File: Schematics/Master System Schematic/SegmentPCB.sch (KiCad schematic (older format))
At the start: 28 parts, among them K13 Voltage Tap Relay, K14 Voltage Tap Relay, K15 Voltage Tap Relay, K16 Voltage Tap Relay, K17 Voltage Tap Relay, K18 Voltage Tap Relay, K19 Voltage Tap Relay, K20 Voltage Tap Relay, K21 Voltage Tap Relay, K22 Voltage Tap Relay

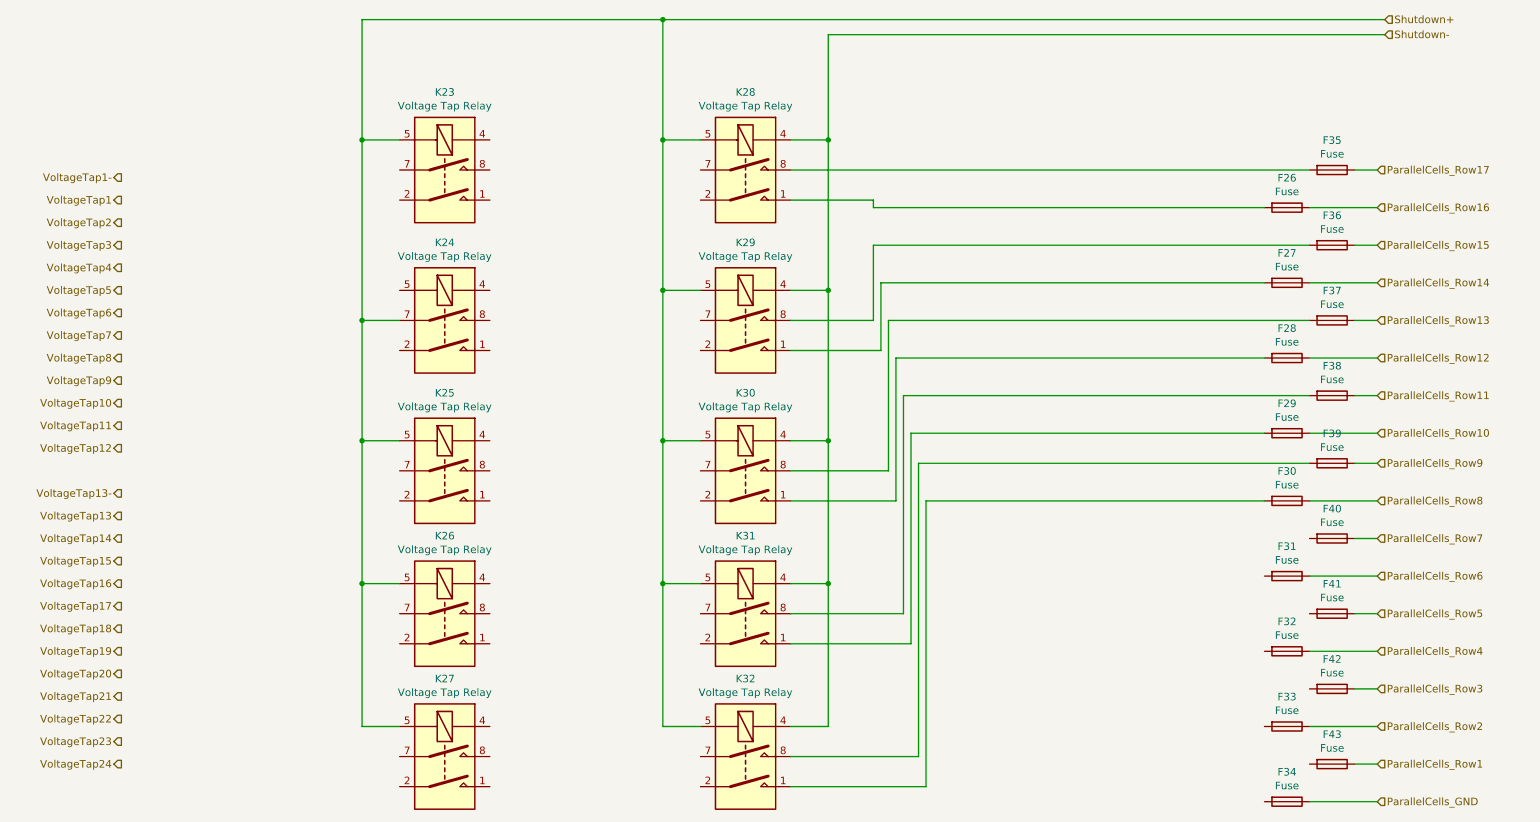
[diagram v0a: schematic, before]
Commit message: Clean up for merge
>cleaned wire runs on top sheet
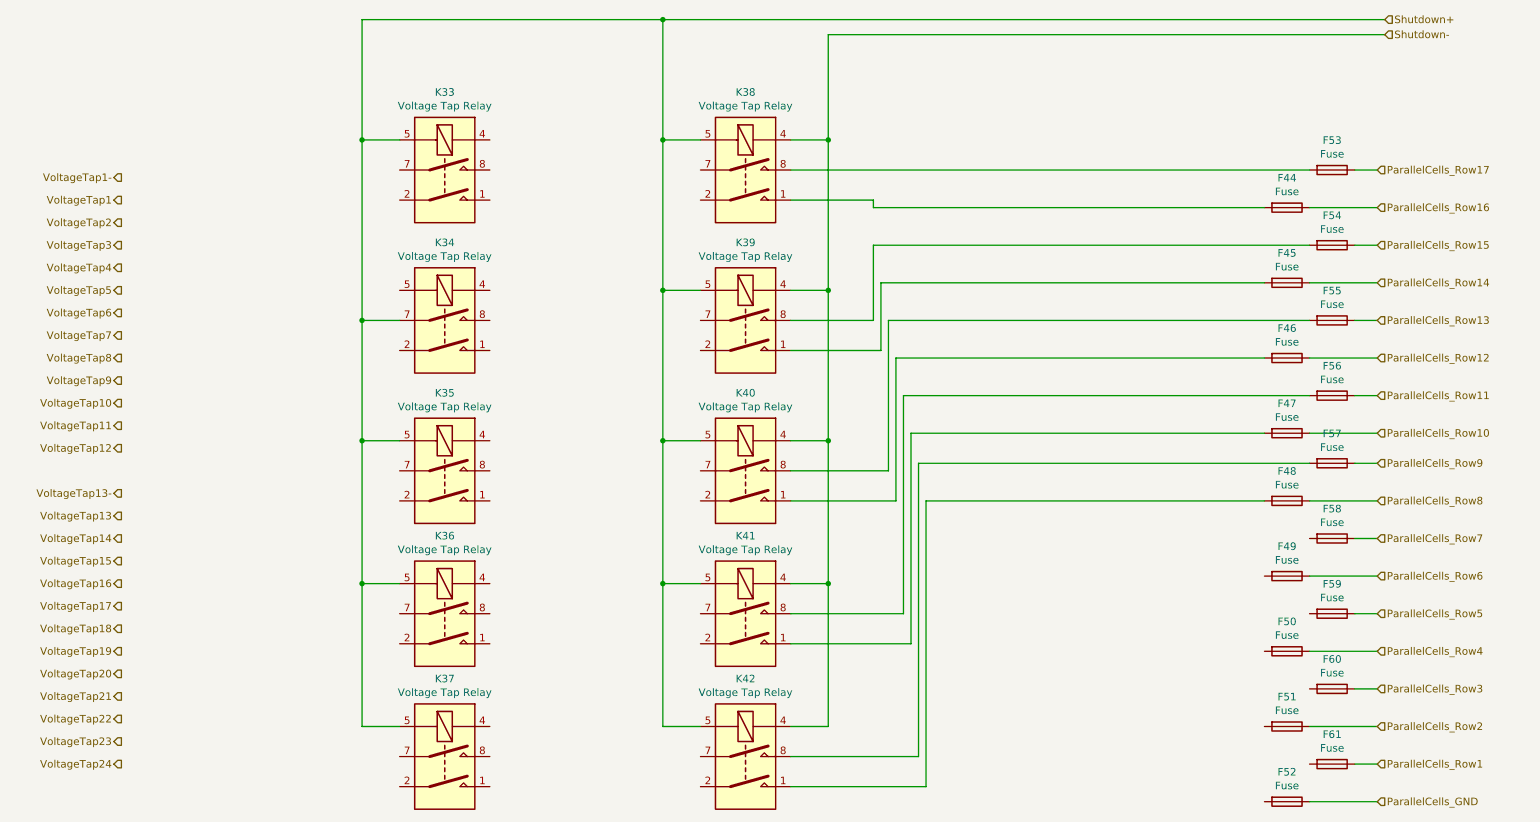
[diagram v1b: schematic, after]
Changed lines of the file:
@@
 EESchema Schematic File Version 4
-LIBS:Master System Schematic-cache
 EELAYER 30 0
 EELAYER END
@@
 AR Path="/5F45B05E/604E5331/6054192C" Ref="K33"  Part="1"
 AR Path="/5F45B05E/604E5333/6054192C" Ref="K43"  Part="1"
-F 0 "K23" H 3650 2367 50  0000 C CNN
+F 0 "K33" H 3650 2367 50  0000 C CNN
 F 1 "Voltage Tap Relay" H 3650 2276 50  0000 C CNN
 F 2 "Relay_THT:Relay_DPST_Fujitsu_FTR-F1A" H 3650 1450 50  0001 C CNN
@@
 AR Path="/5F45B05E/604E5331/60548E5D" Ref="K38"  Part="1"
 AR Path="/5F45B05E/604E5333/60548E5D" Ref="K48"  Part="1"
-F 0 "K28" H 5650 2367 50  0000 C CNN
+F 0 "K38" H 5650 2367 50  0000 C CNN
 F 1 "Voltage Tap Relay" H 5650 2276 50  0000 C CNN
 F 2 "Relay_THT:Relay_DPST_Fujitsu_FTR-F1A" H 5650 1450 50  0001 C CNN
@@
 AR Path="/5F45B05E/604E5331/6054A887" Ref="K39"  Part="1"
 AR Path="/5F45B05E/604E5333/6054A887" Ref="K49"  Part="1"
-F 0 "K29" H 5650 3367 50  0000 C CNN
+F 0 "K39" H 5650 3367 50  0000 C CNN
 F 1 "Voltage Tap Relay" H 5650 3276 50  0000 C CNN
 F 2 "Relay_THT:Relay_DPST_Fujitsu_FTR-F1A" H 5650 2450 50  0001 C CNN
@@
 AR Path="/5F45B05E/604E5331/6054A88D" Ref="K40"  Part="1"
 AR Path="/5F45B05E/604E5333/6054A88D" Ref="K50"  Part="1"
-F 0 "K30" H 5650 4367 50  0000 C CNN
+F 0 "K40" H 5650 4367 50  0000 C CNN
 F 1 "Voltage Tap Relay" H 5650 4276 50  0000 C CNN
 F 2 "Relay_THT:Relay_DPST_Fujitsu_FTR-F1A" H 5650 3450 50  0001 C CNN
@@
 AR Path="/5F45B05E/604E5331/6054A893" Ref="K41"  Part="1"
 AR Path="/5F45B05E/604E5333/6054A893" Ref="K51"  Part="1"
-F 0 "K31" H 5650 5317 50  0000 C CNN
+F 0 "K41" H 5650 5317 50  0000 C CNN
 F 1 "Voltage Tap Relay" H 5650 5226 50  0000 C CNN
 F 2 "Relay_THT:Relay_DPST_Fujitsu_FTR-F1A" H 5650 4400 50  0001 C CNN
@@
 AR Path="/5F45B05E/604E5331/6054A899" Ref="K42"  Part="1"
 AR Path="/5F45B05E/604E5333/6054A899" Ref="K52"  Part="1"
-F 0 "K32" H 5650 6267 50  0000 C CNN
+F 0 "K42" H 5650 6267 50  0000 C CNN
 F 1 "Voltage Tap Relay" H 5650 6176 50  0000 C CNN
 F 2 "Relay_THT:Relay_DPST_Fujitsu_FTR-F1A" H 5650 5350 50  0001 C CNN
@@
 AR Path="/5F45B05E/604E5331/6057568E" Ref="F53"  Part="1"
 AR Path="/5F45B05E/604E5333/6057568E" Ref="F71"  Part="1"
-F 0 "F35" V 9353 1850 50  0000 C CNN
+F 0 "F53" V 9353 1850 50  0000 C CNN
 F 1 "Fuse" V 9444 1850 50  0000 C CNN
 F 2 "" V 9480 1850 50  0001 C CNN
@@
 AR Path="/5F45B05E/604E5331/6057794E" Ref="F54"  Part="1"
 AR Path="/5F45B05E/604E5333/6057794E" Ref="F72"  Part="1"
-F 0 "F36" V 9353 2350 50  0000 C CNN
+F 0 "F54" V 9353 2350 50  0000 C CNN
 F 1 "Fuse" V 9444 2350 50  0000 C CNN
 F 2 "" V 9480 2350 50  0001 C CNN
@@
 AR Path="/5F45B05E/604E5331/60577954" Ref="F45"  Part="1"
 AR Path="/5F45B05E/604E5333/60577954" Ref="F63"  Part="1"
-F 0 "F27" V 9053 2600 50  0000 C CNN
+F 0 "F45" V 9053 2600 50  0000 C CNN
 F 1 "Fuse" V 9144 2600 50  0000 C CNN
 F 2 "" V 9180 2600 50  0001 C CNN
@@
 AR Path="/5F45B05E/604E5331/60579EA8" Ref="F55"  Part="1"
 AR Path="/5F45B05E/604E5333/60579EA8" Ref="F73"  Part="1"
-F 0 "F37" V 9353 2850 50  0000 C CNN
+F 0 "F55" V 9353 2850 50  0000 C CNN
 F 1 "Fuse" V 9444 2850 50  0000 C CNN
 F 2 "" V 9480 2850 50  0001 C CNN
@@
 AR Path="/5F45B05E/604E5331/60579EAE" Ref="F46"  Part="1"
 AR Path="/5F45B05E/604E5333/60579EAE" Ref="F64"  Part="1"
-F 0 "F28" V 9053 3100 50  0000 C CNN
+F 0 "F46" V 9053 3100 50  0000 C CNN
 F 1 "Fuse" V 9144 3100 50  0000 C CNN
 F 2 "" V 9180 3100 50  0001 C CNN
@@
 AR Path="/5F45B05E/604E5331/60579EB6" Ref="F56"  Part="1"
 AR Path="/5F45B05E/604E5333/60579EB6" Ref="F74"  Part="1"
-F 0 "F38" V 9353 3350 50  0000 C CNN
+F 0 "F56" V 9353 3350 50  0000 C CNN
 F 1 "Fuse" V 9444 3350 50  0000 C CNN
 F 2 "" V 9480 3350 50  0001 C CNN
@@
 AR Path="/5F45B05E/604E5331/60579EBC" Ref="F47"  Part="1"
 AR Path="/5F45B05E/604E5333/60579EBC" Ref="F65"  Part="1"
-F 0 "F29" V 9053 3600 50  0000 C CNN
+F 0 "F47" V 9053 3600 50  0000 C CNN
 F 1 "Fuse" V 9144 3600 50  0000 C CNN
 F 2 "" V 9180 3600 50  0001 C CNN
@@
 AR Path="/5F45B05E/604E5331/6057BB2B" Ref="F57"  Part="1"
 AR Path="/5F45B05E/604E5333/6057BB2B" Ref="F75"  Part="1"
-F 0 "F39" V 9353 3800 50  0000 C CNN
+F 0 "F57" V 9353 3800 50  0000 C CNN
 F 1 "Fuse" V 9444 3800 50  0000 C CNN
 F 2 "" V 9480 3800 50  0001 C CNN
@@
 AR Path="/5F45B05E/604E5331/6057BB31" Ref="F48"  Part="1"
 AR Path="/5F45B05E/604E5333/6057BB31" Ref="F66"  Part="1"
-F 0 "F30" V 9053 4050 50  0000 C CNN
+F 0 "F48" V 9053 4050 50  0000 C CNN
 F 1 "Fuse" V 9144 4050 50  0000 C CNN
 F 2 "" V 9180 4050 50  0001 C CNN
@@
 AR Path="/5F45B05E/604E5331/6057BB39" Ref="F58"  Part="1"
 AR Path="/5F45B05E/604E5333/6057BB39" Ref="F76"  Part="1"
-F 0 "F40" V 9353 4300 50  0000 C CNN
+F 0 "F58" V 9353 4300 50  0000 C CNN
 F 1 "Fuse" V 9444 4300 50  0000 C CNN
 F 2 "" V 9480 4300 50  0001 C CNN
@@
 AR Path="/5F45B05E/604E5331/6057BB3F" Ref="F49"  Part="1"
 AR Path="/5F45B05E/604E5333/6057BB3F" Ref="F67"  Part="1"
-F 0 "F31" V 9053 4550 50  0000 C CNN
+F 0 "F49" V 9053 4550 50  0000 C CNN
 F 1 "Fuse" V 9144 4550 50  0000 C CNN
 F 2 "" V 9180 4550 50  0001 C CNN
@@
 AR Path="/5F45B05E/604E5331/6057BB47" Ref="F59"  Part="1"
 AR Path="/5F45B05E/604E5333/6057BB47" Ref="F77"  Part="1"
-F 0 "F41" V 9353 4800 50  0000 C CNN
+F 0 "F59" V 9353 4800 50  0000 C CNN
 F 1 "Fuse" V 9444 4800 50  0000 C CNN
 F 2 "" V 9480 4800 50  0001 C CNN
@@
 AR Path="/5F45B05E/604E5331/6057BB4D" Ref="F50"  Part="1"
 AR Path="/5F45B05E/604E5333/6057BB4D" Ref="F68"  Part="1"
-F 0 "F32" V 9053 5050 50  0000 C CNN
+F 0 "F50" V 9053 5050 50  0000 C CNN
 F 1 "Fuse" V 9144 5050 50  0000 C CNN
 F 2 "" V 9180 5050 50  0001 C CNN
@@
 AR Path="/5F45B05E/604E5331/6057BB55" Ref="F60"  Part="1"
 AR Path="/5F45B05E/604E5333/6057BB55" Ref="F78"  Part="1"
-F 0 "F42" V 9353 5300 50  0000 C CNN
+F 0 "F60" V 9353 5300 50  0000 C CNN
 F 1 "Fuse" V 9444 5300 50  0000 C CNN
 F 2 "" V 9480 5300 50  0001 C CNN
@@
 AR Path="/5F45B05E/604E5331/6057BB5B" Ref="F51"  Part="1"
 AR Path="/5F45B05E/604E5333/6057BB5B" Ref="F69"  Part="1"
-F 0 "F33" V 9053 5550 50  0000 C CNN
+F 0 "F51" V 9053 5550 50  0000 C CNN
 F 1 "Fuse" V 9144 5550 50  0000 C CNN
 F 2 "" V 9180 5550 50  0001 C CNN
@@
 AR Path="/5F45B05E/604E5331/6057D363" Ref="F61"  Part="1"
 AR Path="/5F45B05E/604E5333/6057D363" Ref="F79"  Part="1"
-F 0 "F43" V 9353 5800 50  0000 C CNN
+F 0 "F61" V 9353 5800 50  0000 C CNN
 F 1 "Fuse" V 9444 5800 50  0000 C CNN
 F 2 "" V 9480 5800 50  0001 C CNN
@@
 AR Path="/5F45B05E/604E5331/6057D369" Ref="F52"  Part="1"
 AR Path="/5F45B05E/604E5333/6057D369" Ref="F70"  Part="1"
-F 0 "F34" V 9053 6050 50  0000 C CNN
+F 0 "F52" V 9053 6050 50  0000 C CNN
 F 1 "Fuse" V 9144 6050 50  0000 C CNN
 F 2 "" V 9180 6050 50  0001 C CNN
@@
 AR Path="/5F45B05E/604E5331/60575FDA" Ref="F44"  Part="1"
 AR Path="/5F45B05E/604E5333/60575FDA" Ref="F62"  Part="1"
-F 0 "F26" V 9053 2100 50  0000 C CNN
+F 0 "F44" V 9053 2100 50  0000 C CNN
 F 1 "Fuse" V 9144 2100 50  0000 C CNN
 F 2 "" V 9180 2100 50  0001 C CNN
@@
 AR Path="/5F45B05E/604E5331/605448E5" Ref="K37"  Part="1"
 AR Path="/5F45B05E/604E5333/605448E5" Ref="K47"  Part="1"
-F 0 "K27" H 3650 6267 50  0000 C CNN
+F 0 "K37" H 3650 6267 50  0000 C CNN
 F 1 "Voltage Tap Relay" H 3650 6176 50  0000 C CNN
 F 2 "Relay_THT:Relay_DPST_Fujitsu_FTR-F1A" H 3650 5350 50  0001 C CNN
@@
 AR Path="/5F45B05E/604E5331/6054435E" Ref="K36"  Part="1"
 AR Path="/5F45B05E/604E5333/6054435E" Ref="K46"  Part="1"
-F 0 "K26" H 3650 5317 50  0000 C CNN
+F 0 "K36" H 3650 5317 50  0000 C CNN
 F 1 "Voltage Tap Relay" H 3650 5226 50  0000 C CNN
 F 2 "Relay_THT:Relay_DPST_Fujitsu_FTR-F1A" H 3650 4400 50  0001 C CNN
@@
 AR Path="/5F45B05E/604E5331/60543EA1" Ref="K35"  Part="1"
 AR Path="/5F45B05E/604E5333/60543EA1" Ref="K45"  Part="1"
-F 0 "K25" H 3650 4367 50  0000 C CNN
+F 0 "K35" H 3650 4367 50  0000 C CNN
 F 1 "Voltage Tap Relay" H 3650 4276 50  0000 C CNN
 F 2 "Relay_THT:Relay_DPST_Fujitsu_FTR-F1A" H 3650 3450 50  0001 C CNN
@@
 AR Path="/5F45B05E/604E5331/6054391B" Ref="K34"  Part="1"
 AR Path="/5F45B05E/604E5333/6054391B" Ref="K44"  Part="1"
-F 0 "K24" H 3650 3367 50  0000 C CNN
+F 0 "K34" H 3650 3367 50  0000 C CNN
 F 1 "Voltage Tap Relay" H 3650 3276 50  0000 C CNN
 F 2 "Relay_THT:Relay_DPST_Fujitsu_FTR-F1A" H 3650 2450 50  0001 C CNN
